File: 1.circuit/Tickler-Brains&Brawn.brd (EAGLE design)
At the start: 96.5 x 71.1 mm, 29 parts, among them IC1 MCP23S17SP, J1 PN61729-S, U1 PIC18F4550_40, X1 20Mhz

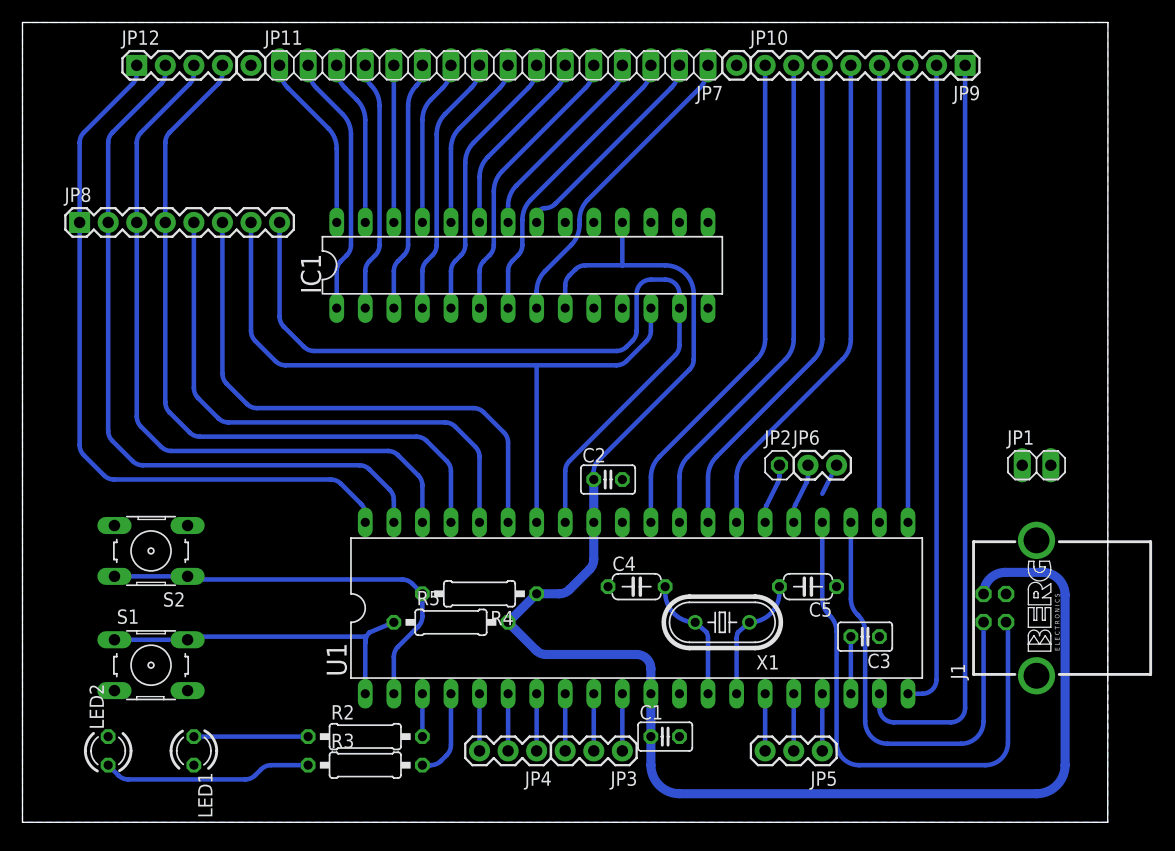
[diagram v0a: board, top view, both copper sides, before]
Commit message: updated pcb to include improvements after building v1 board. software changed to include i2c comms to the expander. not working yet.
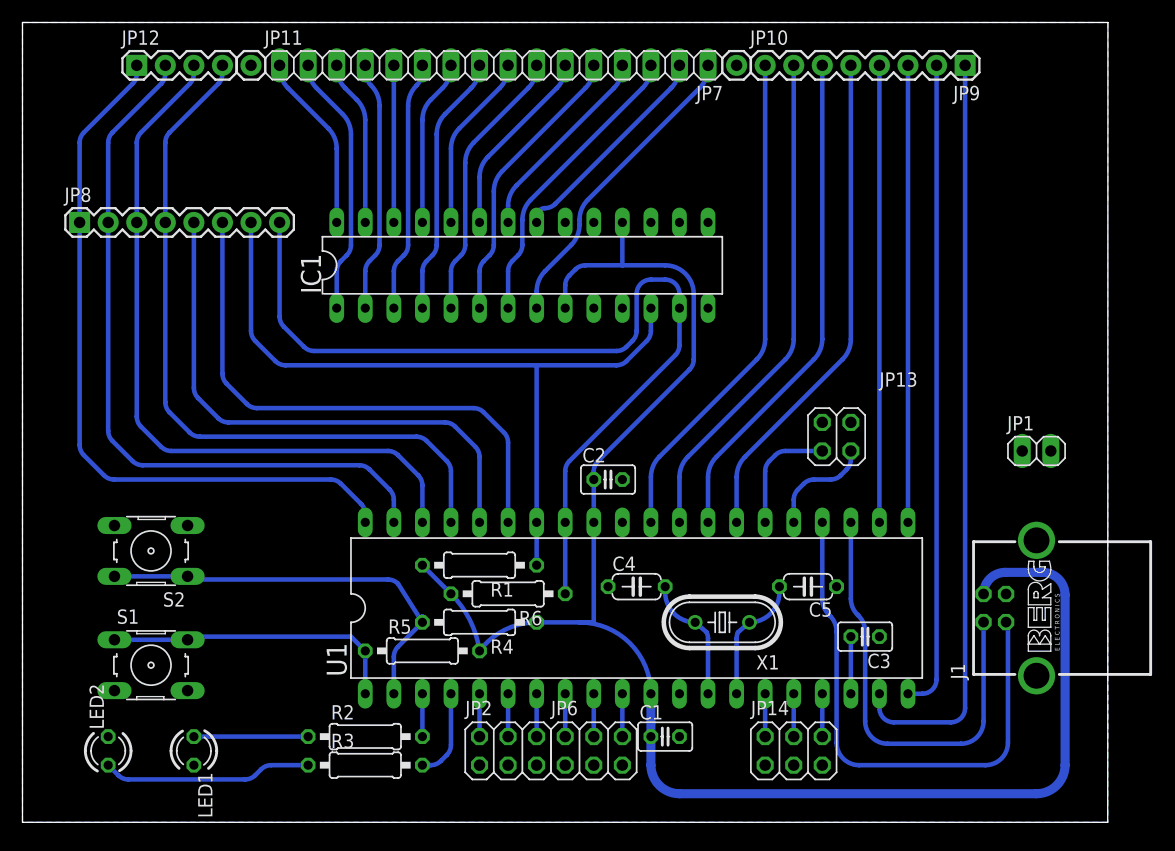
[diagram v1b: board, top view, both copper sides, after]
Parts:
- removed JP3, JP4, JP5: (no value), SparkFun:1X03
- added JP13: Scope trig / TX, pinhead:2X02
- added JP14: (no value), pinhead:2X03
- added R1, R6: 3K3, rcl:0207/10
- IC1: value MCP23S17SP -> MCP23017
- JP2: value trig -> (none); device pinhead:1X01 -> pinhead:2X03
- JP6: value tx -> (none); device SparkFun:1X02 -> pinhead:2X03
- moved JP2 35.0 mm to (31.8, 6.35)
- moved JP6 31.8 mm to (39.4, 6.35)
- moved R5 3.59 mm to (24.1, 15.2)
- moved R4 2.54 mm to (29.2, 17.8)
- moved JP1 1.27 mm to (78.7, 33.0)
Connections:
- net +5V: now also R1.2, R6.2
- net GND: now also JP13.2, JP13.4, JP14.1, JP14.3, JP14.5, JP2.1, JP2.3, JP2.5, JP6.1, JP6.3, JP6.5; no longer JP6.2
- net N$12: now also JP6.6; no longer JP3.1
- net N$13: now also JP6.4; no longer JP3.2
- net N$14: now also JP6.2; no longer JP3.3
- net N$15: now also JP2.6; no longer JP4.1
- net N$16: now also JP2.4; no longer JP4.2
- net N$17: now also JP2.2; no longer JP4.3
- net N$18: now also JP14.6; no longer JP5.1
- net N$19: now also JP14.4; no longer JP5.2
- net N$20: now also JP14.2; no longer JP5.3
- net SCL: now also R1.1
- net SCOPETRIG: now also JP13.1; no longer JP2.1
- net SDA: now also R6.1
- net TX: now also JP13.3; no longer JP6.1
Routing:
- net +5V: track 142.3 -> 150.2 mm
- net SDA: track 74.9 -> 81.3 mm
- net SCOPETRIG: track 5.35 -> 10.5 mm
- net TX: track 5.35 -> 9.62 mm
- net !RESET: track 30.8 -> 26.7 mm
- net SCL: track 64.0 -> 67.8 mm
- net GND: track 2.84 -> 0.00 mm
- net N$20: track 5.08 -> 3.81 mm
- net N$19: track 5.08 -> 3.81 mm
- net N$18: track 5.08 -> 3.81 mm
- net N$17: track 5.08 -> 3.81 mm
- net N$16: track 5.08 -> 3.81 mm
- net N$15: track 5.08 -> 3.81 mm
- net N$14: track 5.08 -> 3.81 mm
- net N$13: track 5.08 -> 3.81 mm
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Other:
- board text added: "Scope trig TX"
